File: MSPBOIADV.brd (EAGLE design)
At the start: 104.1 x 139.4 mm, 23 parts, among them IC1 W25Q32JVDAIQ, U1 MSP430G2553IRHB32T, U2 MSP430G2553IRHB32T

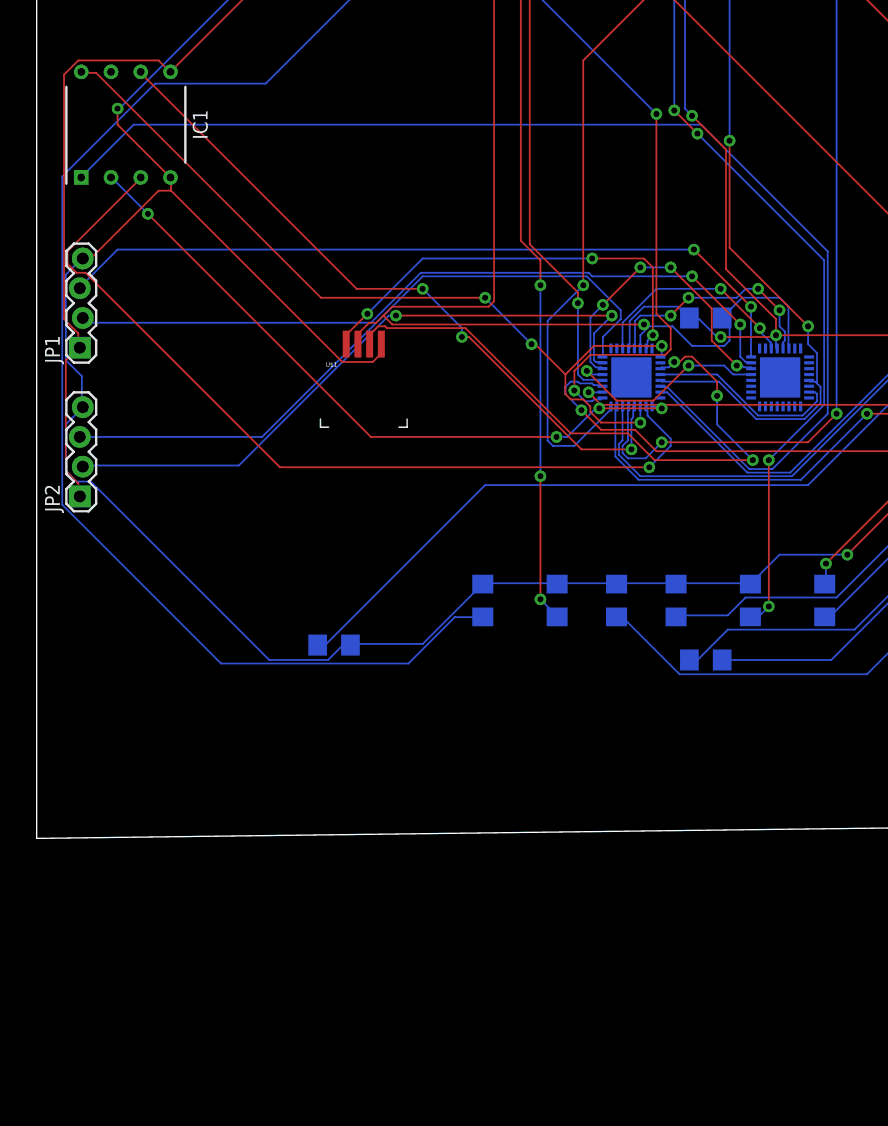
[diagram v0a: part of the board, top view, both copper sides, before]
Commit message: Add files via upload
Fixed board, added 28 pin MSP, and through hole flash chip
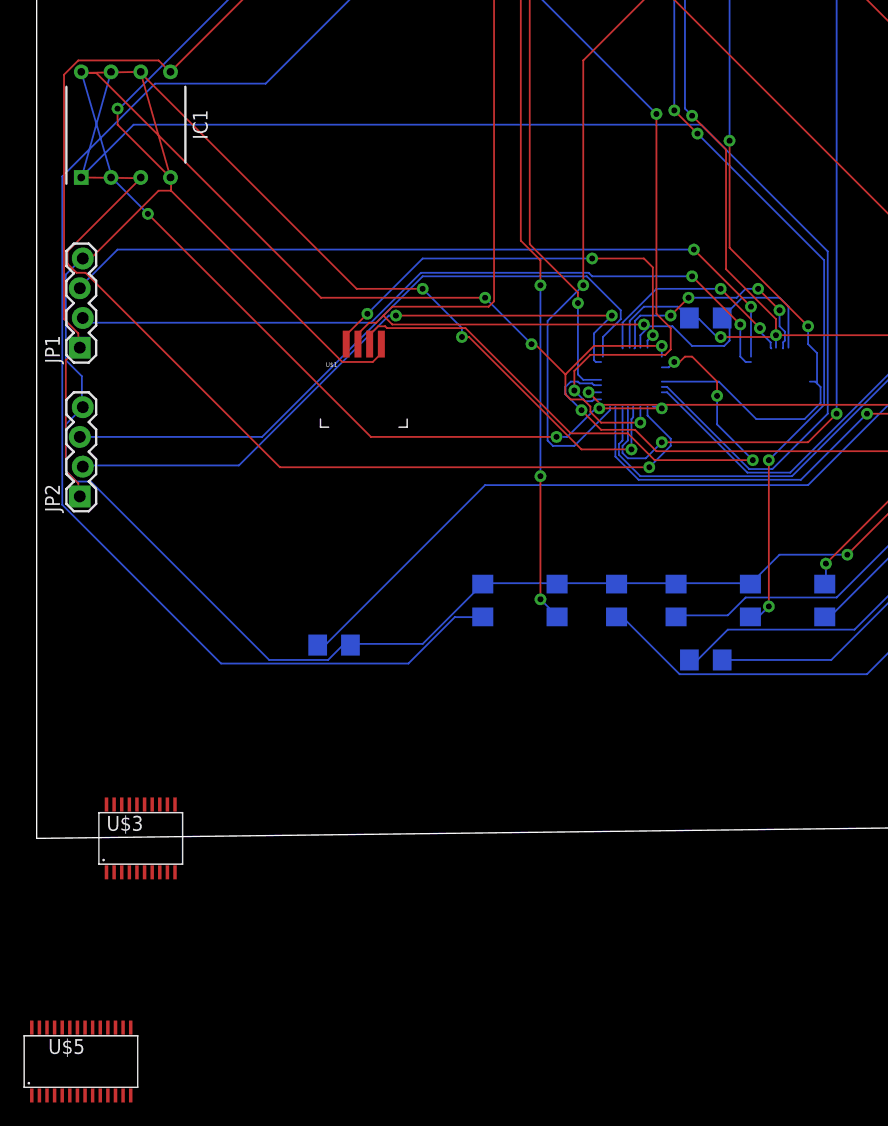
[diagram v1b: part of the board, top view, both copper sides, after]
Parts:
- removed U1, U2: MSP430G2553IRHB32T, ELEC327:RHB32_3P45X3P45
- added U$3: MSP430G2XX3TSSOP, ELEC327:PW20
- added U$5: USETHIS, TI_MSP430_v16:PW28
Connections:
- removed net AVCC: U1.29, U2.29
- removed net AVSS: U1.27, U2.27
- removed net CLOCK: IC1.7
- removed net DATA_FLASH: IC1.2, U2.9
- removed net DATA_INPUT: IC1.8, U2.1, U2.11
- removed net DATA_OUTPUT: U2.2
- removed net DB7: U$2.P$15, U2.16
- new net N$11: U$5.11
- new net N$12: U$5.12
- new net N$13: U$5.13
- new net N$14: U$5.14
- new net O_CLK: IC1.6, U$5.6
- new net O_SIMO: IC1.5, U$5.4
- new net O_SOMI: IC1.2, U$5.3
- net A0: now also U$5.18
- net BTN1: now also U$5.20; no longer U2.19
- net BTN2: now also U$3.13; no longer U2.18
- net C86: now also U$5.21; no longer U2.20
- net CHP_SLCT: now also U$3.8; no longer U1.7, U2.4
- net CS1: now also U$5.9; no longer U2.7
- net CS_FLASH: now also U$5.8; no longer U2.6
- net E/RD: now also U$5.16; no longer U2.15
- net GND: now also U$3.20, U$5.28; no longer U1.28, U2.28
- net HOLD: now also IC1.7, U$5.10, U$5.27; no longer IC1.6, U2.12
- net P/S: now also U$5.26; no longer U2.17
- net RES: now also U$5.15; no longer U2.13
- net RST: now also U$3.16; no longer U1.23
- net RST2: now also U$5.24; no longer U2.23
- net RW/WR: now also U$5.17; no longer U2.14
- net S_CLK_SPI: now also U$3.7, U$5.7; no longer U1.5, U2.5
- net S_SIMO: now also U$2.P$15, U$3.15, U$5.23; no longer U1.22, U2.22
- net S_SOMI: now also U$3.14, U$5.22; no longer U1.21, U2.21
- net TEST: now also U$3.17; no longer U1.24
- net TEST2: now also U$5.25; no longer U2.24
- net VCC: now also IC1.8, U$3.1, U$5.1; no longer IC1.5, U1.30, U2.30
- net WRITE_PROTC: now also U$5.19; no longer U2.10
- net X: now also U$5.2; no longer U2.31
- net Y: now also U$5.5; no longer U2.3
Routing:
- net O_CLK: track 0.00 -> 77.9 mm, vias 0 -> 4
- net WRITE_PROTC: track 73.7 -> 0.00 mm, vias 1 -> 0
- net DATA_INPUT: track 73.1 -> 0.00 mm, vias 4 -> 0
- net GND: track 351.2 -> 419.4 mm, vias 5 -> 8
- net VCC: track 247.1 -> 314.1 mm, vias 3 -> 7
- net DB7: track 61.6 -> 0.00 mm, vias 2 -> 0
- net DATA_FLASH: track 58.1 -> 0.00 mm, vias 4 -> 0
- net HOLD: track 59.6 -> 112.2 mm, vias 3 -> 0
- net S_SIMO: track 25.8 -> 61.5 mm, vias 4 -> 2
- net CS_FLASH: track 103.2 -> 78.6 mm, vias 0 -> 1
- net S_SOMI: track 18.1 -> 0.00 mm, vias 2 -> 0
- net CHP_SLCT: track 16.7 -> 0.00 mm
